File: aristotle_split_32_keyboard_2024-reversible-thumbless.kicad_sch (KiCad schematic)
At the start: 39 parts, among them J1 8P8C, J2 Screw_Terminal_01x04, J3 Screw_Terminal_01x04, K13 SW_SPDT, K14 SW_SPDT, K15 SW_SPDT, K16 SW_SPDT, K17 SW_SPDT, K23 SW_SPDT, K24 SW_SPDT, K25 SW_SPDT, K26 SW_SPDT, K27 SW_SPDT, K4 SW_SPDT, K5 SW_SPDT, K6 SW_SPDT, K7 SW_SPDT, SW1 SW_SPDT, U1 ProMicro_r

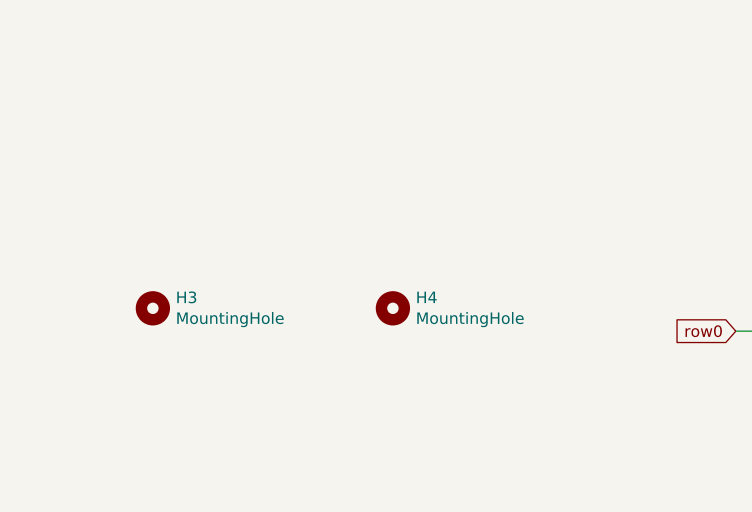
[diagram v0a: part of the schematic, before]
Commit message: Fix mounting holes
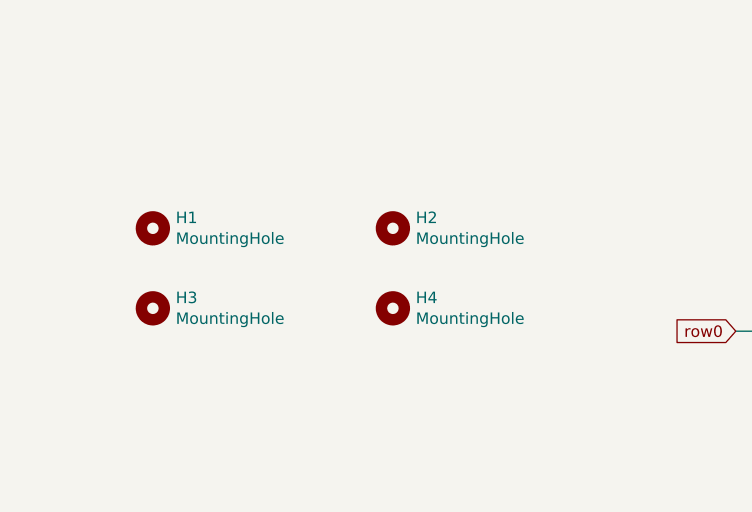
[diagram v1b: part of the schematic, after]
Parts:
- added H1, H2: MountingHole, MountingHole:MountingHole_2.2mm_M2, symbol Mechanical:MountingHole
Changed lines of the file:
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@@
+    )
+  )
+  (symbol (lib_id "Mechanical:MountingHole") (at 29.21 58.42 0) (unit 1)
+    (in_bom yes) (on_board yes) (dnp no)
+    (property "Reference" "H1" (at 31.75 57.2516 0)
+      (effects (font (size 1.27 1.27)) (justify left))
+    )
+    (property "Value" "MountingHole" (at 31.75 59.563 0)
+      (effects (font (size 1.27 1.27)) (justify left))
+    )
+    (property "Footprint" "MountingHole:MountingHole_2.2mm_M2" (at 29.21 58.42 0)
+      (effects (font (size 1.27 1.27)) hide)
+    )
+    (property "Datasheet" "~" (at 29.21 58.42 0)
+      (effects (font (size 1.27 1.27)) hide)
+    )
+    (instances
+      (project "aristotle_split_32_keyboard_2024-reversible-thumbless"
+        (path "/31e08896-1992-4725-96d9-9d2728bca7a3"
+          (reference "H1") (unit 1)
+        )
+      )
     )
   )
@@
         )
       )
+    )
+  )
+  (symbol (lib_id "Mechanical:MountingHole") (at 55.88 58.42 0) (unit 1)
+    (in_bom yes) (on_board yes) (dnp no)
+    (property "Reference" "H2" (at 58.42 57.2516 0)
+      (effects (font (size 1.27 1.27)) (justify left))
+    )
+    (property "Value" "MountingHole" (at 58.42 59.563 0)
+      (effects (font (size 1.27 1.27)) (justify left))
+    )
+    (property "Footprint" "MountingHole:MountingHole_2.2mm_M2" (at 55.88 58.42 0)
+      (effects (font (size 1.27 1.27)) hide)
+    )
+    (property "Datasheet" "~" (at 55.88 58.42 0)
+      (effects (font (size 1.27 1.27)) hide)
+    )
+    (instances
+      (project "aristotle_split_32_keyboard_2024-reversible-thumbless"
+        (path "/31e08896-1992-4725-96d9-9d2728bca7a3"
+          (reference "H2") (unit 1)
+        )
+      )
